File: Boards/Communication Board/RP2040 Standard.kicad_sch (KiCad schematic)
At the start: 37 parts, among them J1 BM03B-SRSS-TBLFSN, J6 USB_C, SW2 SW_Push, SW6 SW_Push, U1 ESD7L5.0DT5G, U5 ST1L05APU33R

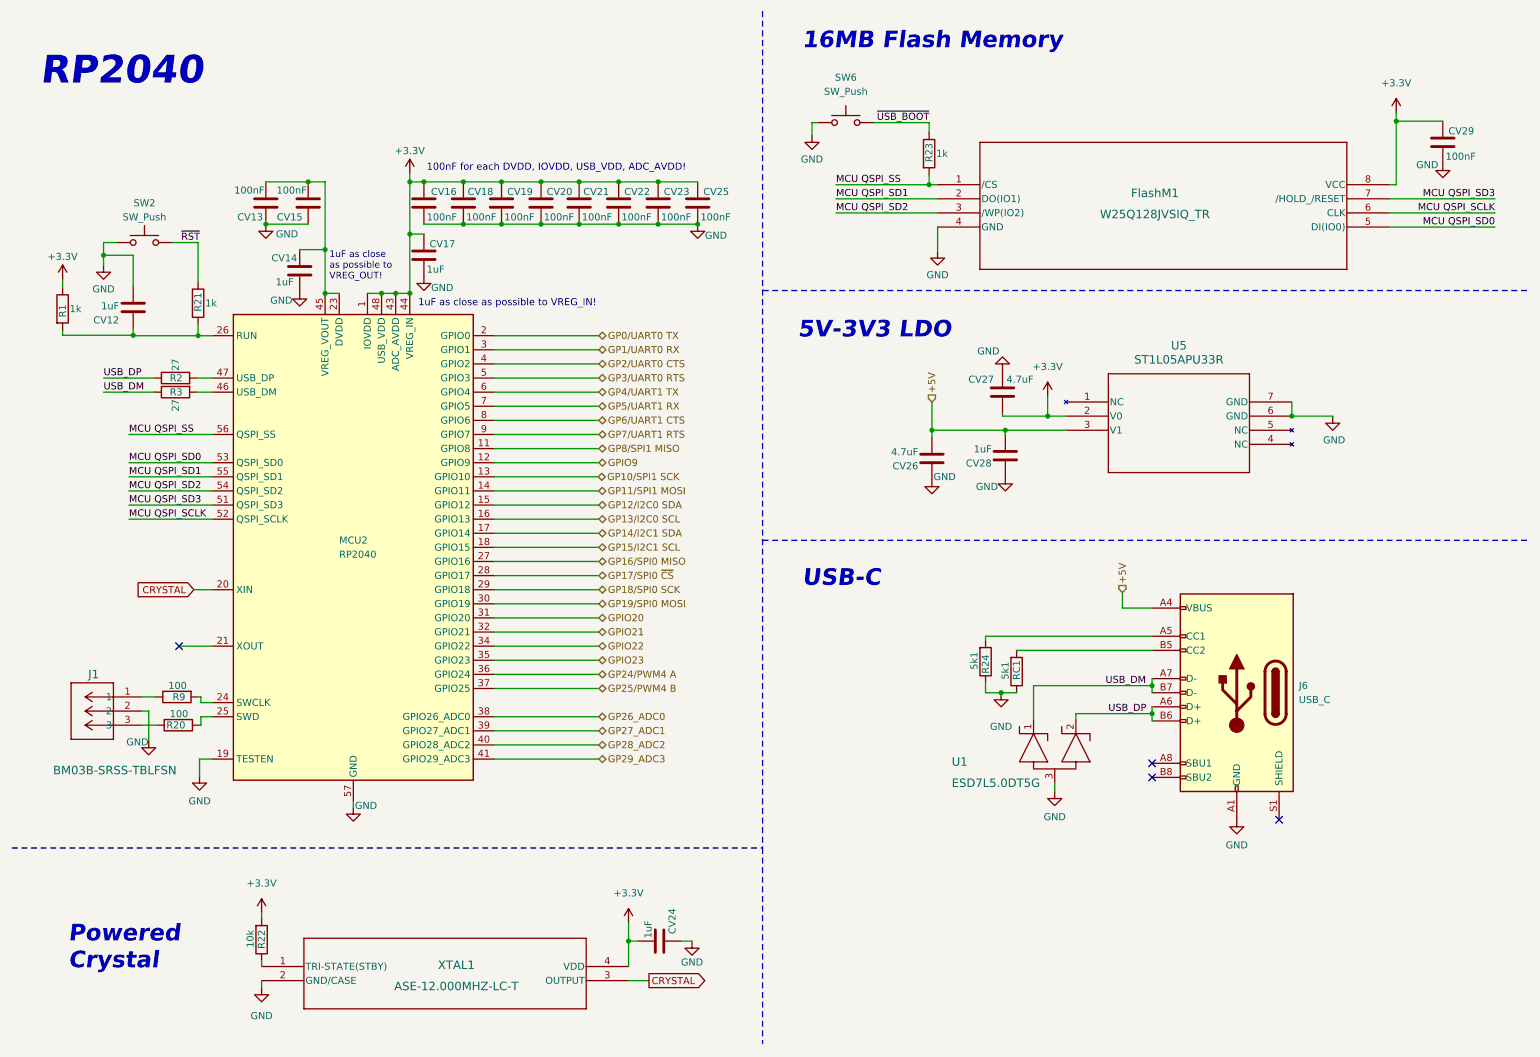
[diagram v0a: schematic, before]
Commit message: Correção de erros ERC na Communication Board
Foram corrigidos todos os erros e avisos ERC na Communication Board.
Foram feitas alterações aos ficheiros de alguns símbolos e adicionou-se
um Schottky Diode de proteção
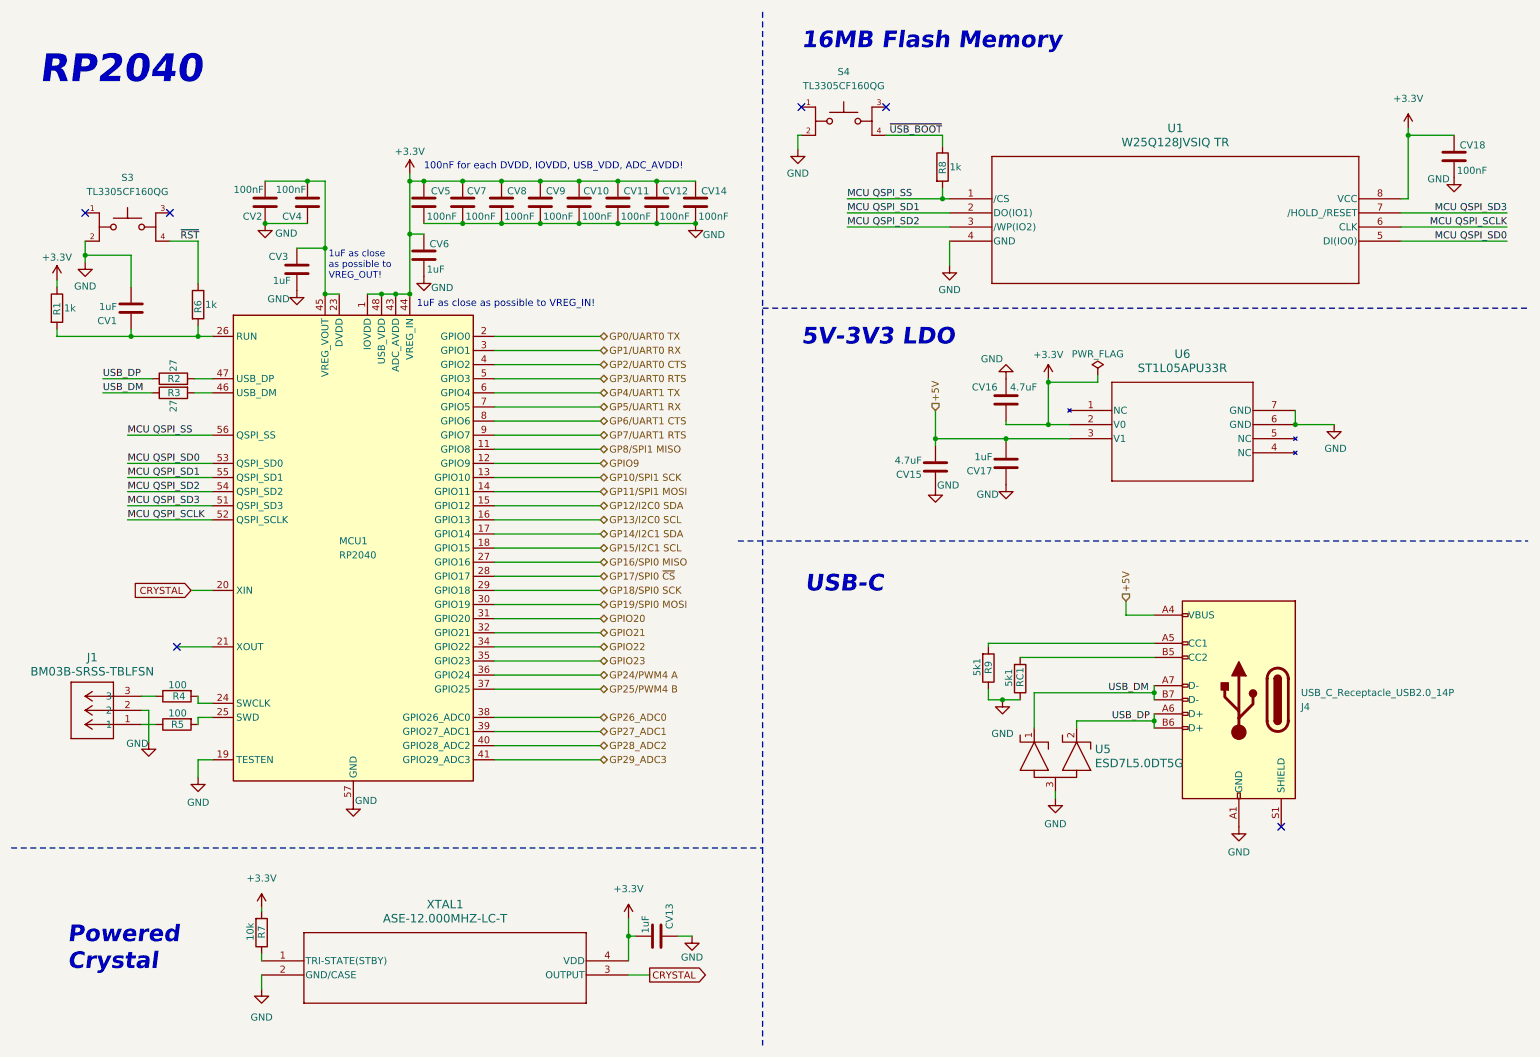
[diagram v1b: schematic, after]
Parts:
- removed CV19, CV20, CV21, CV22, CV23, CV25, CV29: 100nF, Capacitor_SMD:C_0201_0603Metric, symbol Device:C
- removed CV24, CV28: 1uF, Capacitor_SMD:C_0201_0603Metric, symbol Device:C
- removed CV26, CV27: 4.7uF, Capacitor_SMD:C_0201_0603Metric, symbol Device:C
- removed FlashM1: W25Q128JVSIQ_TR, SOIC_208MIL_WIN, symbol W25Q128JVSIQ TR:W25Q128JVSIQ_TR
- removed J1: BM03B-SRSS-TBLFSN, CONN_BM03B-SRSS-TBLFSN_JST, symbol SWD Con:BM03B-SRSS-TBLFSN
- removed J6: USB_C, Connector_USB:USB_C_Plug_JAE_DX07P024AJ1, symbol Connector:USB_C_Receptacle_USB2.0
- removed MCU2: RP2040, Package_DFN_QFN:QFN-56-1EP_7x7mm_P0.4mm_EP3.2x3.2mm, symbol MCU_RaspberryPi:RP2040
- removed R20: 100, Resistor_SMD:R_0201_0603Metric, symbol Device:R
- removed R21, R23: 1k, Resistor_SMD:R_0201_0603Metric, symbol Device:R
- removed R22: 10k, Resistor_SMD:R_0201_0603Metric, symbol Device:R
- removed R24: 5k1, Resistor_SMD:R_0201_0603Metric, symbol Device:R
- removed SW2, SW6: SW_Push, Button_Switch_SMD:SW_Push_1P1T-MP_NO_Horizontal_Alps_SKRTLAE010, symbol Switch:SW_Push
- removed U1: ESD7L5.0DT5G, SOT-723_0P85X1P25_ONS, symbol ESD Protection Diode:ESD7L5.0DT5G
- removed U5: ST1L05APU33R, DFN_5APU33R_STM, symbol LDO 5V.3V3:ST1L05APU33R
- removed XTAL1: ASE-12.000MHZ-LC-T, ASE-3.2X2.5_ABR, symbol AS12MHz:ASE-12.000MHZ-LC-T
- added CV1, CV3, CV6: 1uF, Capacitor_SMD:C_0201_0603Metric, symbol Device:C
- added CV10, CV11, CV2, CV4, CV5, CV7, CV8, CV9: 100nF, Capacitor_SMD:C_0201_0603Metric, symbol Device:C
- added J1: BM03B-SRSS-TBLFSN, CONN_BM03B-SRSS-TBLFSN_JST, symbol SWD Connector:BM03B-SRSS-TBLFSN
- added J4: USB_C_Receptacle_USB2.0_14P, symbol Connector:USB_C_Receptacle_USB2.0_14P
- added MCU1: RP2040, Package_DFN_QFN:QFN-56-1EP_7x7mm_P0.4mm_EP3.2x3.2mm, symbol MCU_RaspberryPi:RP2040
- added R4, R5: 100, Resistor_SMD:R_0201_0603Metric, symbol Device:R
- added R6, R8: 1k, Resistor_SMD:R_0201_0603Metric, symbol Device:R
- added R7: 10k, Resistor_SMD:R_0201_0603Metric, symbol Device:R
- added S3, S4: TL3305CF160QG, TL3305CF160QG:SW_TL3305CF160QG, symbol TL3305CF160QG:TL3305CF160QG
- added U1: W25Q128JVSIQ TR, SOIC_208MIL_WIN, symbol 16MB Flash Memory:W25Q128JVSIQ_TR
- added U5: ESD7L5.0DT5G, SOT-723_0P85X1P25_ONS, symbol ESD Diodes:ESD7L5.0DT5G
- added U6: ST1L05APU33R, DFN_5APU33R_STM, symbol LDO 5V 3V3:ST1L05APU33R
- added XTAL1: ASE-12.000MHZ-LC-T, ASE-3.2X2.5_ABR, symbol Powered Crystal:ASE-12.000MHZ-LC-T
- CV12, CV14: value 1uF -> 100nF
- CV13: value 100nF -> 1uF
- CV15, CV16: value 100nF -> 4.7uF
- R9: value 100 -> 5k1
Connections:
- net +3.3V: now also CV12.1, CV13.1, CV14.1, CV16.2, CV10.1, CV11.1, CV5.1, CV6.1, CV7.1, CV8.1, CV9.1, MCU1.1 (IOVDD), MCU1.10 (IOVDD), MCU1.22 (IOVDD), MCU1.33 (IOVDD), MCU1.42 (IOVDD), MCU1.43 (ADC_AVDD), MCU1.44 (VREG_IN), MCU1.48 (USB_VDD), MCU1.49 (IOVDD), R7.2, U1.8 (VCC), U6.2 (V0), XTAL1.4 (VDD); no longer CV16.1, CV17.1
- net +5V: now also CV15.2, CV17.2, J4.A4 (VBUS), J4.A9 (VBUS), J4.B4 (VBUS), J4.B9 (VBUS), U6.3 (V1)
- net CRYSTAL: now also MCU1.20 (XIN), XTAL1.3 (OUTPUT)
- net GND: now also CV13.2, CV16.1, CV17.1, R9.1, CV1.2, CV10.2, CV11.2, CV2.1, CV3.2, CV4.1, CV5.2, CV6.2, CV7.2, CV8.2, CV9.2, J1.2, J4.A1 (GND), J4.A12 (GND), J4.B1 (GND), J4.B12 (GND), MCU1.19 (TESTEN), MCU1.57 (GND), S3.2, S4.2, U1.4 (GND), U5.3, U6.6 (GND), U6.7 (GND), XTAL1.2 (GND/CASE); no longer CV13.1, CV16.2, CV17.2
- net GP0/UART0 TX: now also MCU1.2 (GPIO0)
- net GP10/SPI1 SCK: now also MCU1.13 (GPIO10)
- net GP11/SPI1 MOSI: now also MCU1.14 (GPIO11)
- net GP12/I2C0 SDA: now also MCU1.15 (GPIO12)
- net GP13/I2C0 SCL: now also MCU1.16 (GPIO13)
- net GP14/I2C1 SDA: now also MCU1.17 (GPIO14)
- net GP15/I2C1 SCL: now also MCU1.18 (GPIO15)
- net GP16/SPI0 MISO: now also MCU1.27 (GPIO16)
- net GP17/SPI0 ~{CS}: now also MCU1.28 (GPIO17)
- net GP18/SPI0 SCK: now also MCU1.29 (GPIO18)
- net GP19/SPI0 MOSI: now also MCU1.30 (GPIO19)
- net GP1/UART0 RX: now also MCU1.3 (GPIO1)
- net GP24/PWM4 A: now also MCU1.36 (GPIO24)
- net GP25/PWM4 B: now also MCU1.37 (GPIO25)
- net GP26_ADC0: now also MCU1.38 (GPIO26_ADC0)
- net GP27_ADC1: now also MCU1.39 (GPIO27_ADC1)
- net GP28_ADC2: now also MCU1.40 (GPIO28_ADC2)
- net GP29_ADC3: now also MCU1.41 (GPIO29_ADC3)
- net GP2/UART0 CTS: now also MCU1.4 (GPIO2)
- net GP3/UART0 RTS: now also MCU1.5 (GPIO3)
- net GP4/UART1 TX: now also MCU1.6 (GPIO4)
- net GP5/UART1 RX: now also MCU1.7 (GPIO5)
- net GP6/UART1 CTS: now also MCU1.8 (GPIO6)
- net GP7/UART1 RTS: now also MCU1.9 (GPIO7)
- net GP8/SPI1 MISO: now also MCU1.11 (GPIO8)
- net GPIO20: now also MCU1.31 (GPIO20)
- net GPIO21: now also MCU1.32 (GPIO21)
- net GPIO22: now also MCU1.34 (GPIO22)
- net GPIO23: now also MCU1.35 (GPIO23)
- net GPIO9: now also MCU1.12 (GPIO9)
- net MCU QSPI_SCLK: now also MCU1.52 (QSPI_SCLK), U1.6 (CLK)
- net MCU QSPI_SD0: now also MCU1.53 (QSPI_SD0), U1.5 (DI(IO0))
- net MCU QSPI_SD1: now also MCU1.55 (QSPI_SD1), U1.2 (DO(IO1))
- net MCU QSPI_SD2: now also MCU1.54 (QSPI_SD2), U1.3 (/WP(IO2))
- net MCU QSPI_SD3: now also MCU1.51 (QSPI_SD3), U1.7 (/HOLD_/RESET)
- net MCU QSPI_SS: now also MCU1.56 (QSPI_SS), R8.2, U1.1 (/CS)
- net USB_DM: now also J4.A7 (D-), J4.B7 (D-), U5.1
- net USB_DP: now also J4.A6 (D+), J4.B6 (D+), U5.2
- net ~{RST}: now also R6.1, S3.4
- net ~{USB_BOOT}: now also R8.1, S4.4
- net at R9.2: now also J4.A5 (CC1)
- net at R1.2: now also CV1.1, MCU1.26 (RUN), R6.2; no longer CV12.1
- net at R3.2: now also MCU1.46 (USB_DM)
- net at R2.2: now also MCU1.47 (USB_DP)
- net at RC1.2: now also J4.B5 (CC2)
- new net: R7.1, XTAL1.1 (TRI-STATE(STBY))
- new net: CV2.2, CV3.1, CV4.2, MCU1.23 (DVDD), MCU1.45 (VREG_VOUT), MCU1.50 (DVDD)
- new net: MCU1.24 (SWCLK), R4.2
- new net: MCU1.25 (SWD), R5.2
- new net: J1.1, R5.1
- new net: J1.3, R4.1
- no-connect marks 4 -> 6

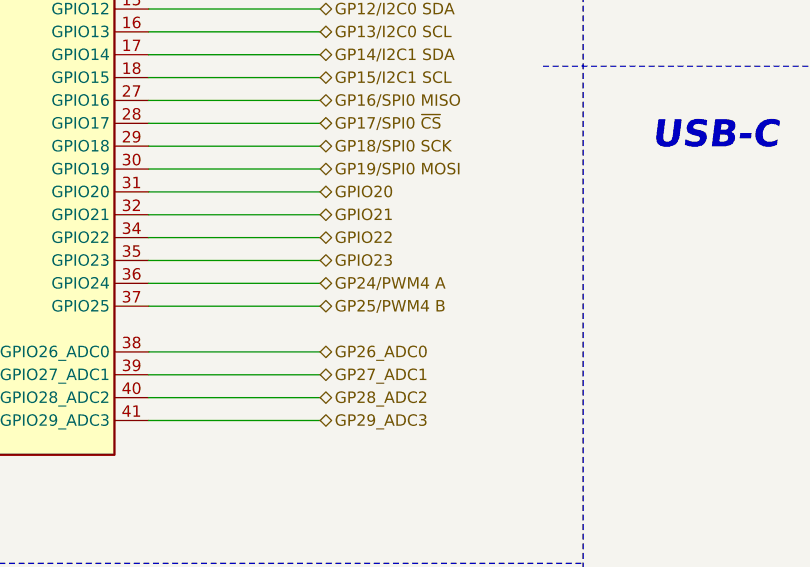
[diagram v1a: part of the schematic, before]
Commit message: pequenas alterações, implementação do sensor de temperatura na placa de comunicações
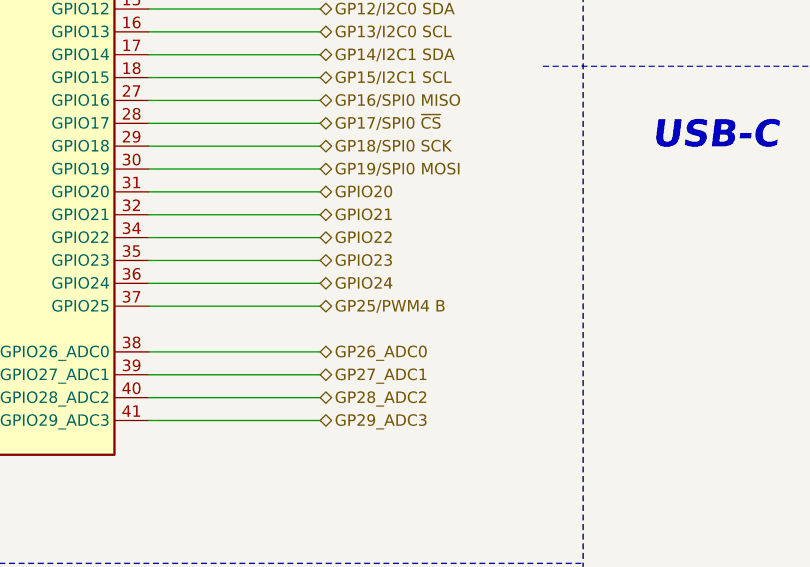
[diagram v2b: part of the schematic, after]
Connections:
- net GP24/PWM4 A renamed GPIO24
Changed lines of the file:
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@@
 		)
 	)
-	(hierarchical_label "GP24{slash}PWM4 A"
+	(hierarchical_label "GPIO24"
 		(shape bidirectional)
 		(at 118.11 131.445 0)

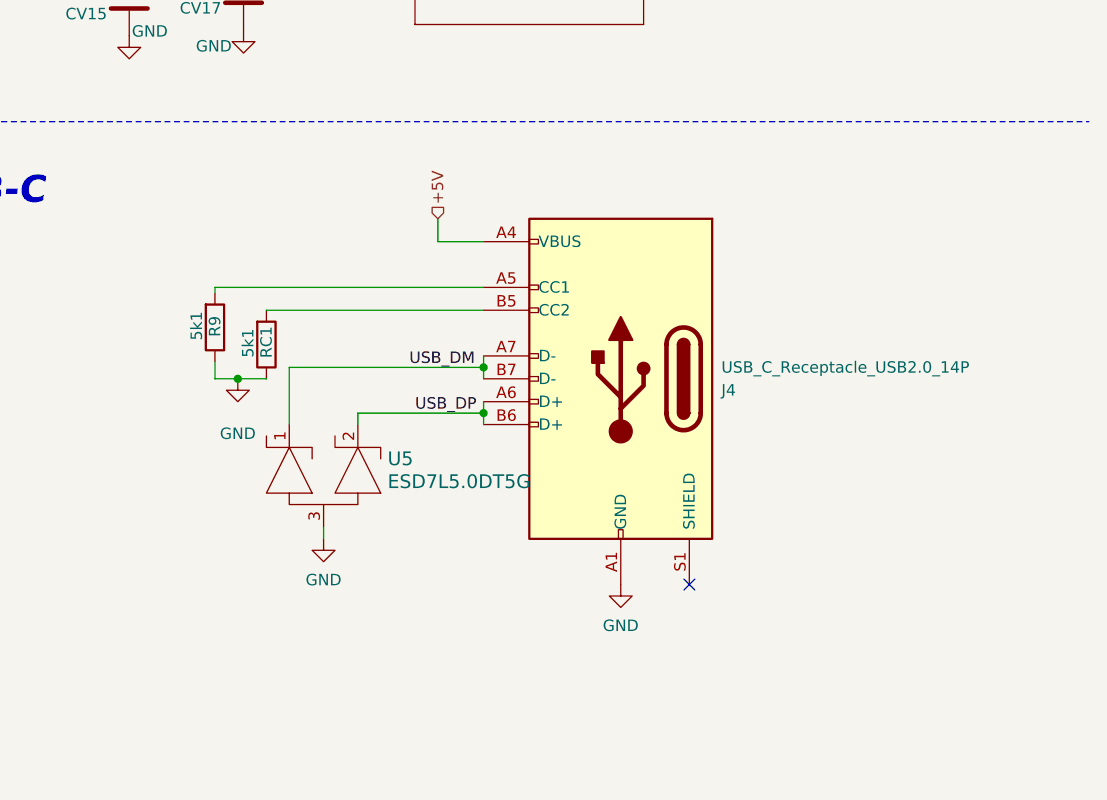
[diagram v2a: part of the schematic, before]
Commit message: USB-C update
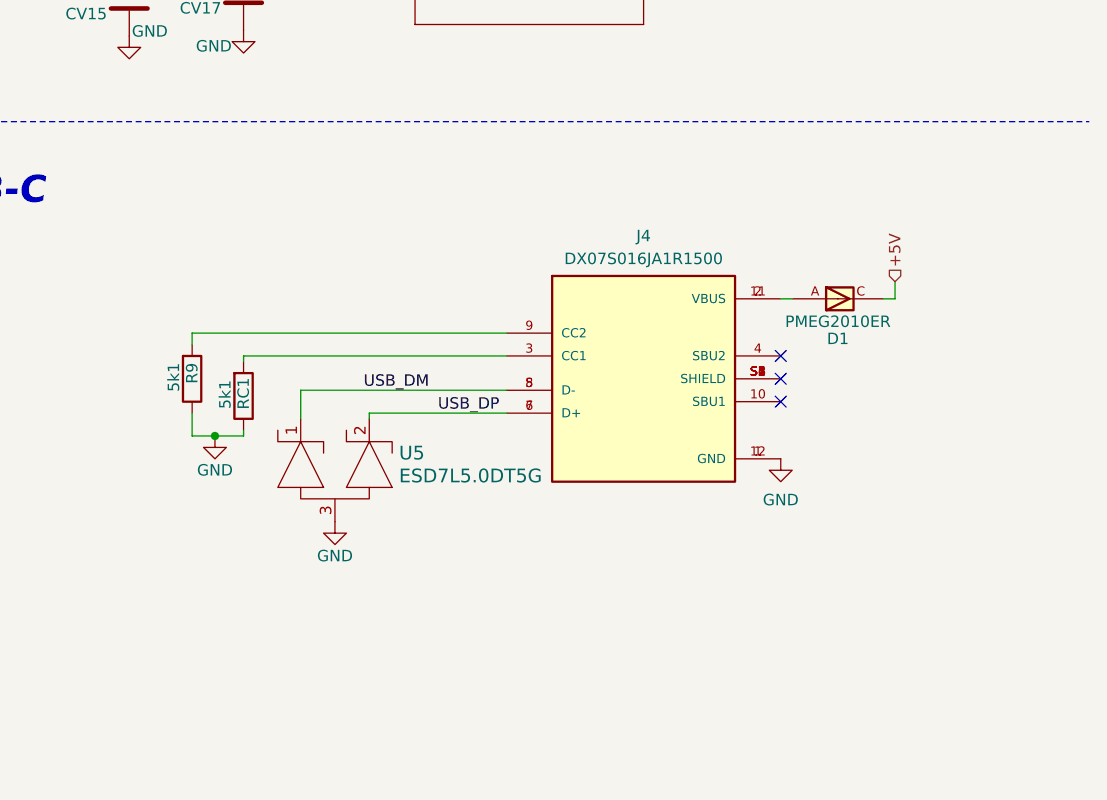
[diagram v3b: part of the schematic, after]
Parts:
- removed J4: USB_C_Receptacle_USB2.0_14P, symbol Connector:USB_C_Receptacle_USB2.0_14P
- added D1: PMEG2010ER, PMEG2010ER:SODFL3517X110N, symbol Schottky Diode:PMEG2010ER
- added J4: DX07S016JA1R1500, DX07S016JA1R1500:JAE_DX07S016JA1R1500, symbol DX07S016JA1R1500:DX07S016JA1R1500
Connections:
- net +5V: now also D1.C
- net GND: now also J4.1 (GND), J4.12 (GND)
- net USB_DM: now also J4.5 (D-), J4.8 (D-)
- net USB_DP: now also J4.6 (D+), J4.7 (D+)
- net at R9.2: now also J4.9 (CC2)
- net at RC1.2: now also J4.3 (CC1)
- new net: D1.A, J4.11 (VBUS), J4.2 (VBUS)
- new net: J4.S1 (SHIELD), J4.S2 (SHIELD), J4.S3 (SHIELD), J4.S4 (SHIELD), J4.S5 (SHIELD), J4.S6 (SHIELD)
- no-connect marks 6 -> 8
